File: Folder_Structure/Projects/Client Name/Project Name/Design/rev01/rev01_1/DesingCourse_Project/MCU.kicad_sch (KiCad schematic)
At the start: 39 parts, among them J1 Conn_01x06_Pin, J2 Conn_01x03_Pin, J3 Conn_01x08_Pin, SW1 SW_DIP_x01, U1 STM32F405RGTx, Y1 8MHz

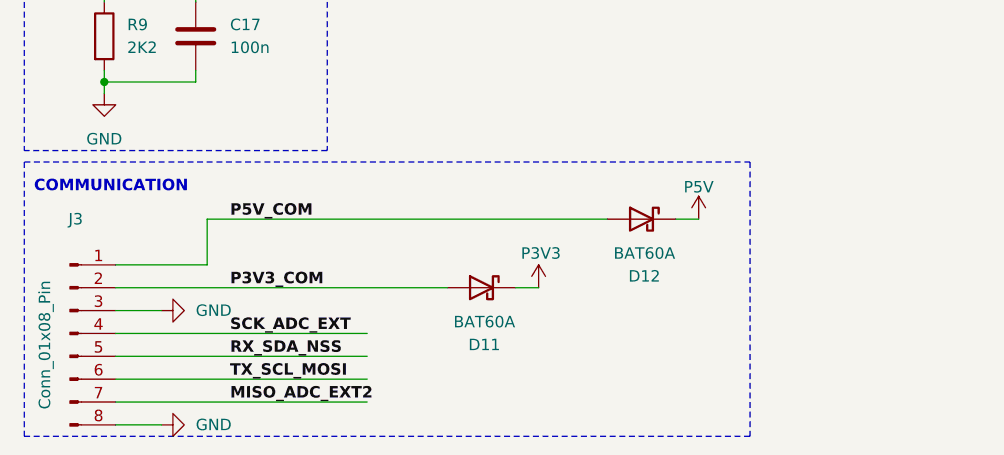
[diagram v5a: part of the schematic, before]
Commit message: Update 10
All done up to MOSFET page, replace all connected to actual PN
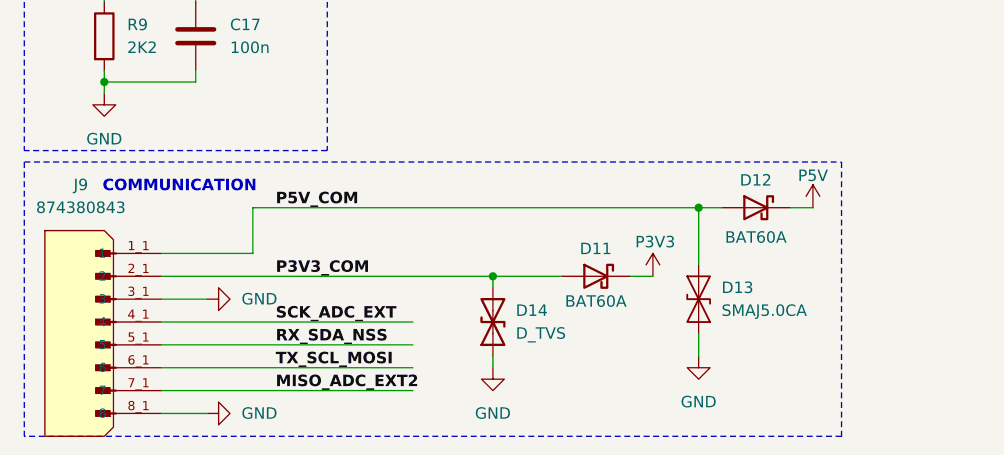
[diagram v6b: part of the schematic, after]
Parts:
- removed J3: Conn_01x08_Pin, symbol Connector:Conn_01x08_Pin
- added D13: SMAJ5.0CA, SMAJ5.0CA:DIOM4325X250N, symbol JGB_Library:SMAJ5.0CA
- added D14: D_TVS, symbol Device:D_TVS
- added J9: 874380843, 874380843:MOLEX_874380843, symbol 874380843:874380843
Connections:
- net GND: now also D13.1 (A1), D14.1 (A1), J9.3_1 (3), J9.3_2 (3), J9.8_1 (8), J9.8_2 (8)
- net MISO_ADC_EXT2: now also J9.7_1 (7), J9.7_2 (7)
- net P3V3_COM: now also D14.2 (A2), J9.2_1 (2), J9.2_2 (2)
- net P5V_COM: now also D13.2 (A2), J9.1_1 (1), J9.1_2 (1)
- net RX_SDA_NSS: now also J9.5_1 (5), J9.5_2 (5)
- net SCK_ADC_EXT: now also J9.4_1 (4), J9.4_2 (4)
- net TX_SCL_MOSI: now also J9.6_1 (6), J9.6_2 (6)
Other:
- moved on the sheet: D11, D12

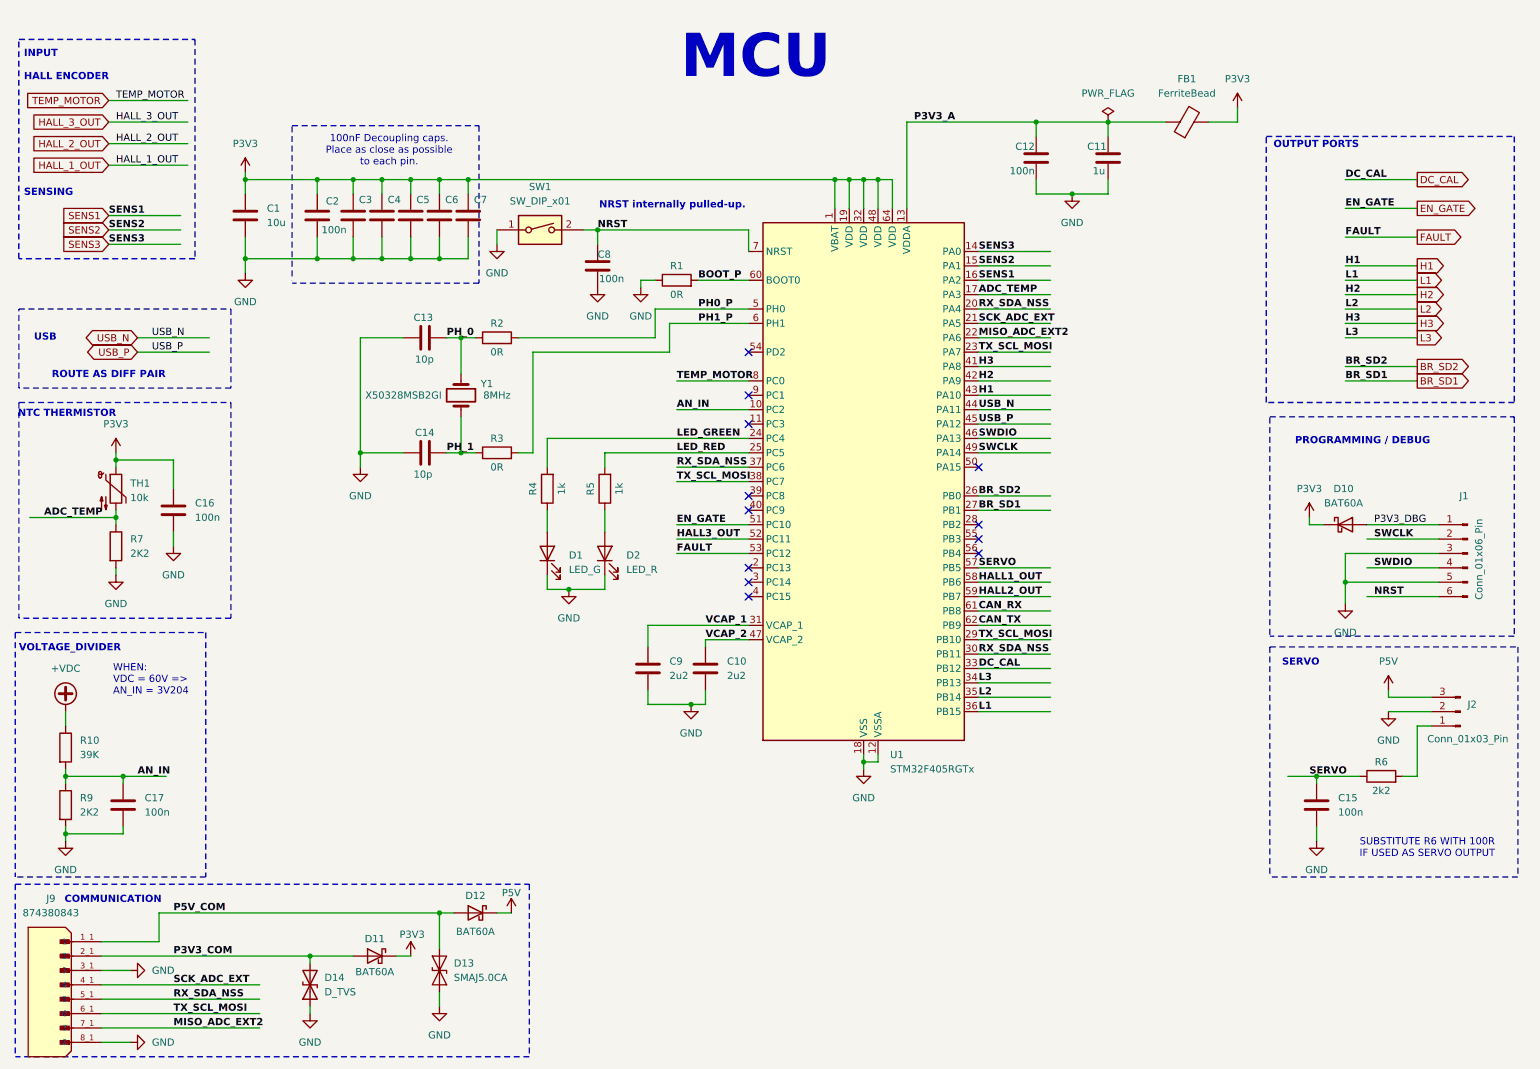
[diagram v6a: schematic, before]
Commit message: Update 11
SCH finishe, missing the labels and logos and adding all passive components
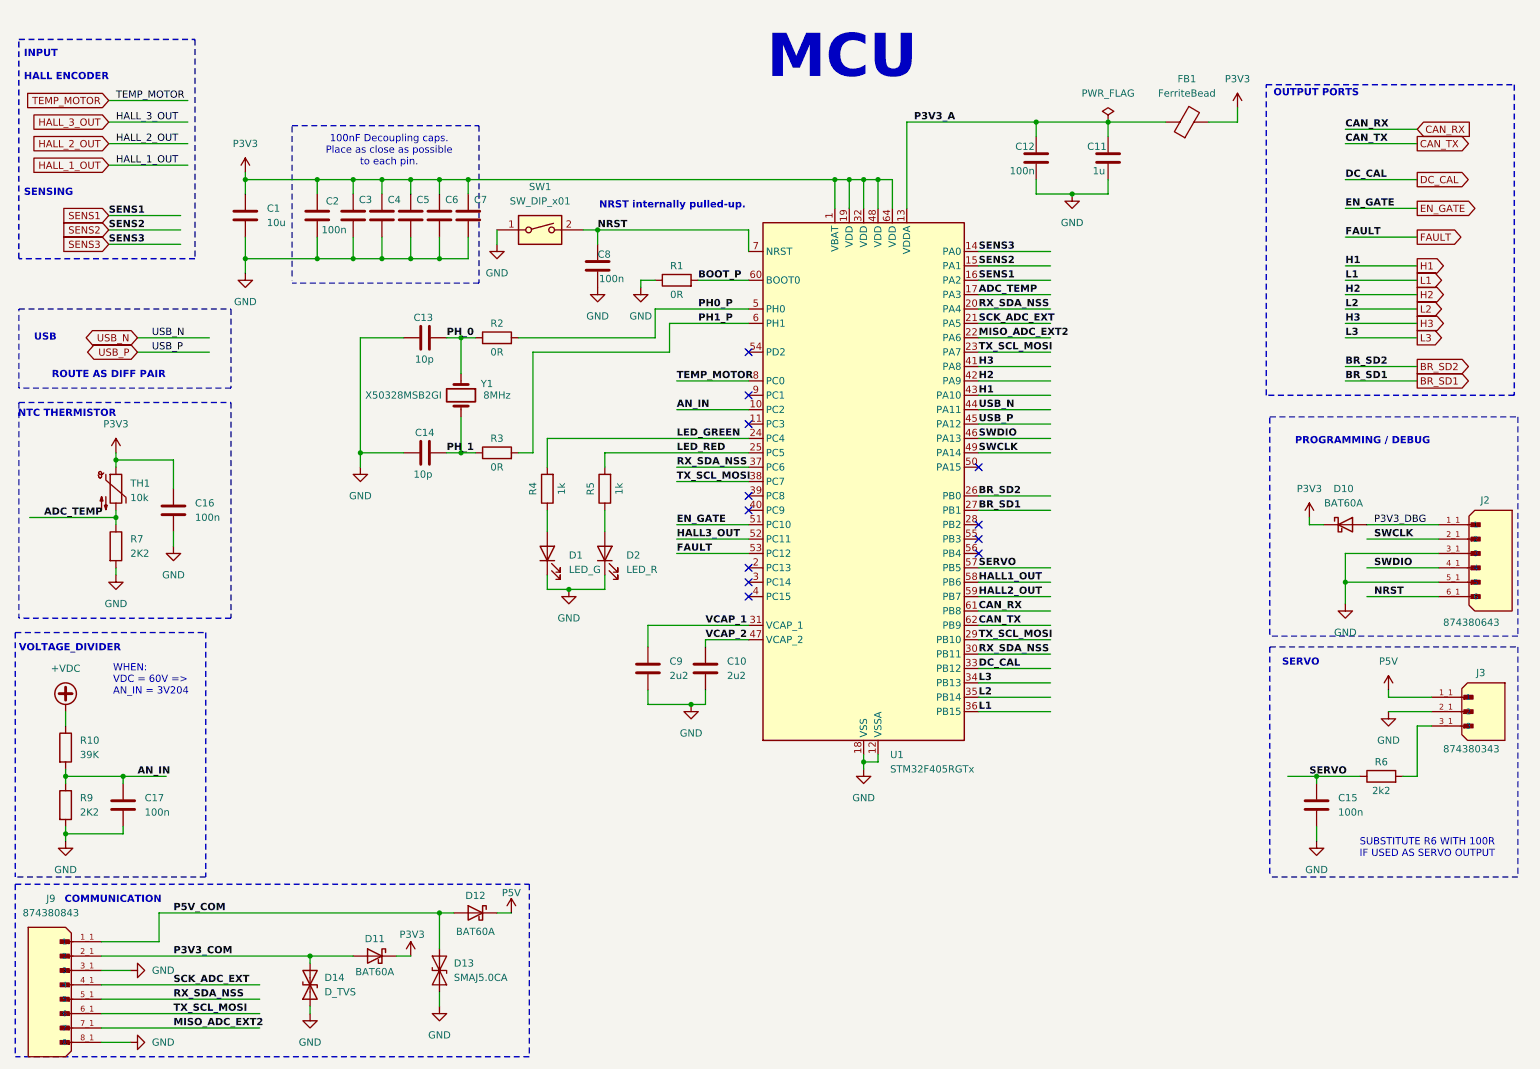
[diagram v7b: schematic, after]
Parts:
- removed J1: Conn_01x06_Pin, symbol Connector:Conn_01x06_Pin
- removed J2: Conn_01x03_Pin, symbol Connector:Conn_01x03_Pin
- added J2: 874380643, 874380843:MOLEX_874380643, symbol Molex_87438:874380643
- added J3: 874380343, 874380843:MOLEX_874380343, symbol Molex_87438:874380343
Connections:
- net GND: now also J2.3_1 (3), J2.3_2 (3), J2.5_1 (5), J2.5_2 (5), J3.2_1 (2), J3.2_2 (2)
- net NRST: now also J2.6_1 (6), J2.6_2 (6)
- net P3V3_DBG: now also J2.1_1 (1), J2.1_2 (1)
- net P5V: now also J3.1_1 (1), J3.1_2 (1)
- net SWCLK: now also J2.2_1 (2), J2.2_2 (2)
- net SWDIO: now also J2.4_1 (4), J2.4_2 (4)
- net at R6.2: now also J3.3_1 (3), J3.3_2 (3)

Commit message: Update 12
Until STEP-DOWN page, all components have complete libraries.

Creation and incluison of all logos and labels libraries
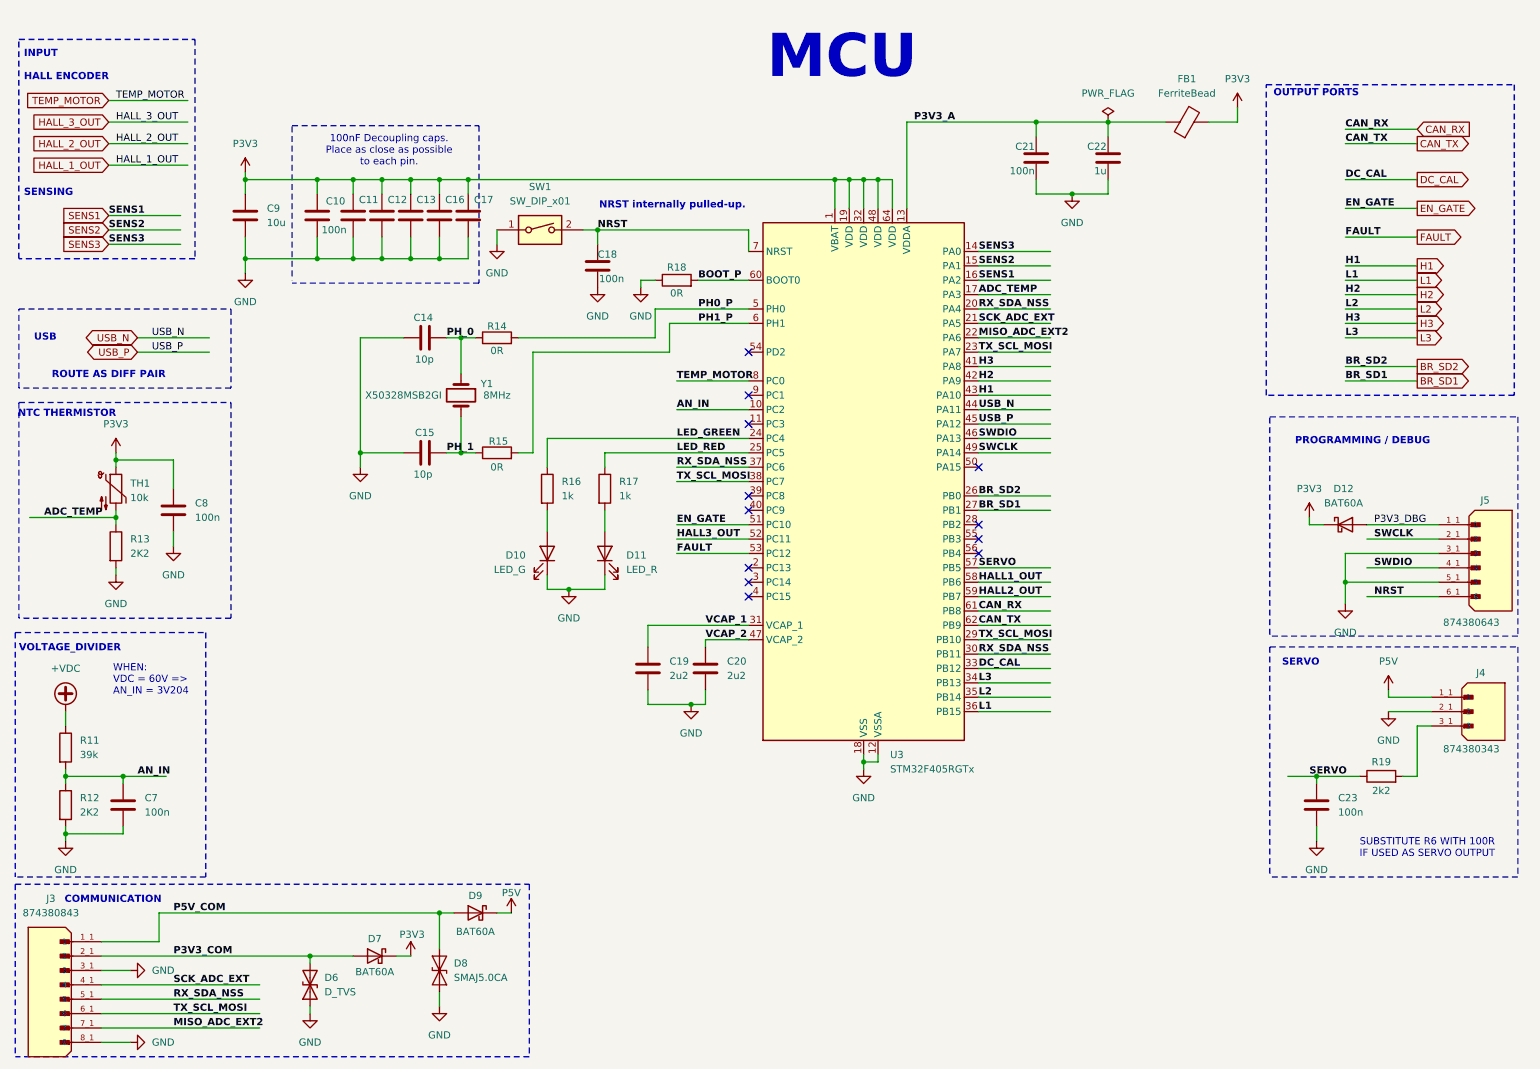
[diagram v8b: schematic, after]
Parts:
- removed C11: 1u, symbol Device:C
- removed D1: LED_G, symbol Device:LED
- removed D2: LED_R, symbol Device:LED
- removed R1, R2, R3: 0R, symbol Device:R
- removed R10: 39K, symbol Device:R
- removed R4, R5: 1k, symbol Device:R
- added C22: 1u, Capacitor_SMD:C_0603_1608Metric, symbol Device:C
- added D10: LED_G, Diode_SMD:D_1206_3216Metric, symbol Device:LED
- added D11: LED_R, Diode_SMD:D_1206_3216Metric, symbol Device:LED
- added R11: 39k, Resistor_SMD:R_0603_1608Metric, symbol Device:R
- added R14, R15, R18: 0R, Resistor_SMD:R_0603_1608Metric, symbol Device:R
- added R16, R17: 1k, Resistor_SMD:R_0603_1608Metric, symbol Device:R
- renumbered C2 to C10, C3 to C11, C4 to C12, C5 to C13, C13 to C14, C14 to C15, C6 to C16, C7 to C17, C8 to C18, C9 to C19, C10 to C20, C12 to C21, C15 to C23, C17 to C7, C16 to C8, C1 to C9, D10 to D12, D14 to D6, D11 to D7, D13 to D8, D12 to D9, J9 to J3, J3 to J4, J2 to J5, R9 to R12, R7 to R13, R6 to R19, U1 to U3
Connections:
- net +VDC: now also R11.1
- net AN_IN: now also R11.2
- net BOOT_P: now also R18.2
- net GND: now also C22.2, D10.1 (K), D11.1 (K), R18.1
- net LED_GREEN: now also R16.1
- net LED_RED: now also R17.1
- net P3V3_A: now also C22.1
- net PH0_P: now also R14.2
- net PH1_P: now also R15.2
- net PH_0: now also R14.1
- net PH_1: now also R15.1
- new net: D11.2 (A), R17.2
- new net: D10.2 (A), R16.2
